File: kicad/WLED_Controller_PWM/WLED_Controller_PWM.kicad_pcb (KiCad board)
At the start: 2 copper layers, 72 x 50 mm, 45 parts, among them J1 USB_C_Receptacle_USB2.0, J2 Conn_01x03, J3 Conn_01x03, J4 Conn_01x03, J6 Conn_01x02, Q1 BC847, Q2 BC847, SW1 SW_RESET, SW2 SW_BOOT, SW3 SW_Push, U1 ESP32-WROOM-32, U2 CH340C, U3 NCP1117-3.3, U4 TSSP58P38, U5 74HC14

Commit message: Add PWM Controllers
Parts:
- removed C13: 100n, Capacitor_SMD:C_0603_1608Metric_Pad1.08x0.95mm_HandSolder
- removed J2, J3, J4: Conn_01x03, GioN_Custom:TerminalBlock_WAGO_236-403_1x03_P5.00mm_45Degree
- removed U5: 74HC14, Package_SO:SOIC-14_3.9x8.7mm_P1.27mm
- added J5: Conn_01x05, GioN_Custom:TerminalBlock_WAGO_236-405_1x05_P5.00mm_45Degree, F.Cu at (9.40, -31.9)
- added Q3: IRFL4105PBF, Package_TO_SOT_SMD:SOT-223, F.Cu at (22.9, -29.2)
- added Q4: IRFL4105PBF, Package_TO_SOT_SMD:SOT-223, F.Cu at (22.9, -21.3)
- added Q5: IRFL4105PBF, Package_TO_SOT_SMD:SOT-223, F.Cu at (22.9, -13.5)
- added Q6: IRFL4105PBF, Package_TO_SOT_SMD:SOT-223, F.Cu at (22.9, -5.59)
- added R13: 100R, Resistor_SMD:R_0603_1608Metric_Pad0.98x0.95mm_HandSolder, F.Cu at (29.0, -32.0)
- added R14: 10k, Resistor_SMD:R_0603_1608Metric_Pad0.98x0.95mm_HandSolder, F.Cu at (29.0, -26.4)
- added R15: 100R, Resistor_SMD:R_0603_1608Metric_Pad0.98x0.95mm_HandSolder, F.Cu at (29.0, -24.1)
- added R16: 10k, Resistor_SMD:R_0603_1608Metric_Pad0.98x0.95mm_HandSolder, F.Cu at (29.0, -18.5)
- added R17: 100R, Resistor_SMD:R_0603_1608Metric_Pad0.98x0.95mm_HandSolder, F.Cu at (29.0, -16.3)
- added R18: 10k, Resistor_SMD:R_0603_1608Metric_Pad0.98x0.95mm_HandSolder, F.Cu at (29.0, -10.7)
- added R19: 100R, Resistor_SMD:R_0603_1608Metric_Pad0.98x0.95mm_HandSolder, F.Cu at (29.0, -8.38)
- added R20: 10k, Resistor_SMD:R_0603_1608Metric_Pad0.98x0.95mm_HandSolder, F.Cu at (29.0, -2.79)
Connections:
- J6 pad 1: +5V -> +12V
- U1 pad 23: LED0 -> LED_R
- U1 pad 27: LED1 -> LED_G
- U1 pad 28: LED2 -> LED_B
- U1 pad 30: IO18 -> LED_W
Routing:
- net +5V: track 195.3 -> 48.2 mm
- net LED1: track 45.6 -> 0.00 mm, vias 2 -> 0
- net +12V: track 0.00 -> 44.9 mm
- net LED2: track 35.5 -> 0.00 mm, vias 2 -> 0
- net LED_G: track 0.00 -> 31.0 mm, vias 0 -> 2
- net LED_W: track 0.00 -> 29.6 mm, vias 0 -> 2
- net Net-(J4-Pin_2): track 27.2 -> 0.00 mm
- net LED_R: track 0.00 -> 26.7 mm, vias 0 -> 2
- net Net-(J3-Pin_2): track 25.8 -> 0.00 mm
- net LED_B: track 0.00 -> 25.0 mm, vias 0 -> 2
- net Net-(J2-Pin_2): track 22.2 -> 0.00 mm
- net Net-(J5-Pin_5): track 0.00 -> 20.9 mm
- net Net-(J5-Pin_4): track 0.00 -> 17.6 mm
- net LED0: track 17.1 -> 0.00 mm, vias 2 -> 0
- net Net-(J5-Pin_2): track 0.00 -> 16.3 mm
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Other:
- board text added: "+12V"
- board text added: "IO15 R"
- board text added: "IO16 G"
- board text added: "IO17 B"
- board text added: "IO18 W"
- board text added: "WLED Controller PWM V1 03/2024 Gioulekas Nikos"
- board text removed: "+5V"
- board text removed: "IO15 LED0"
- board text removed: "IO16 LED1"
- board text removed: "IO17 LED2"
- board text removed: "WLED Controller V1 02/2024 Gioulekas Nikos"

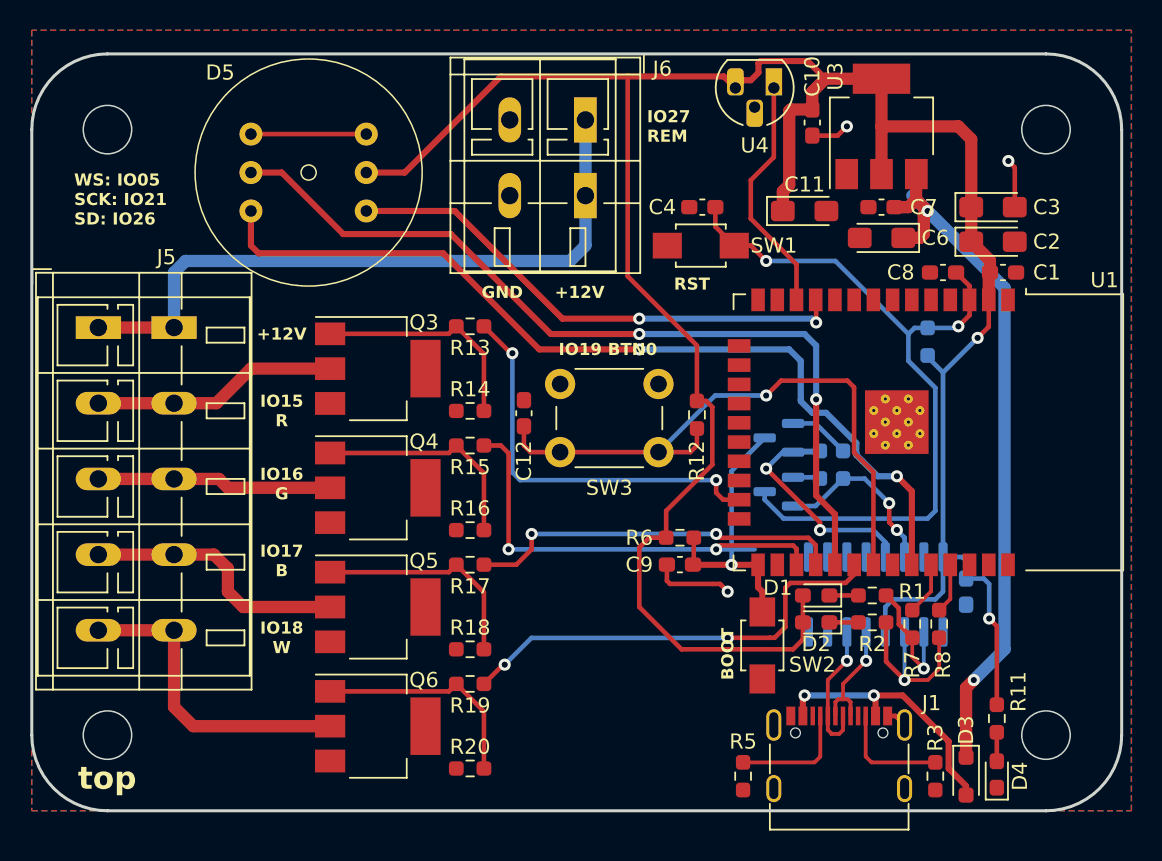
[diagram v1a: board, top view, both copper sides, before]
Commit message: add 7805
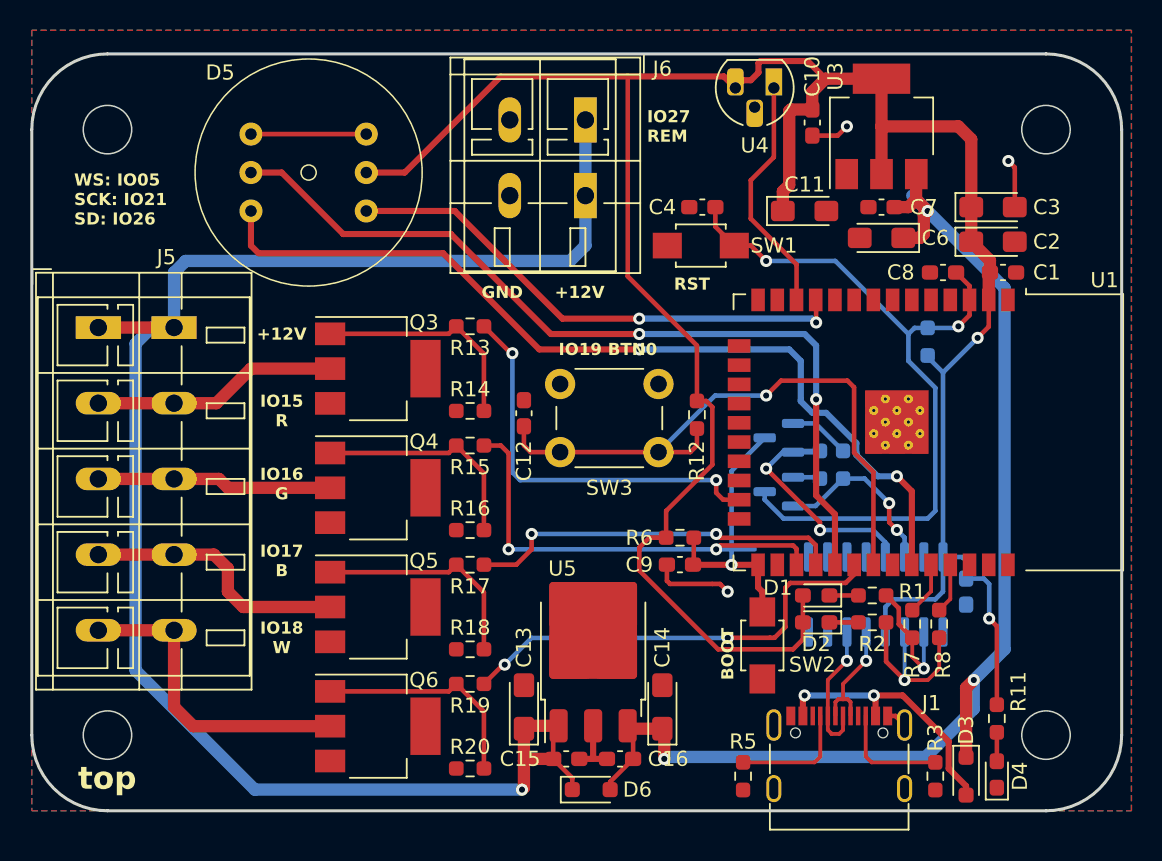
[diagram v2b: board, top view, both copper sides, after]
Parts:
- added C13: 10u, Capacitor_Tantalum_SMD:CP_EIA-3216-18_Kemet-A_Pad1.58x1.35mm_HandSolder, F.Cu at (32.5, -6.86)
- added C14: 10u, Capacitor_Tantalum_SMD:CP_EIA-3216-18_Kemet-A_Pad1.58x1.35mm_HandSolder, F.Cu at (41.7, -6.86)
- added C15: 100n, Capacitor_SMD:C_0603_1608Metric_Pad1.08x0.95mm_HandSolder, F.Cu at (35.3, -3.43)
- added C16: 100n, Capacitor_SMD:C_0603_1608Metric_Pad1.08x0.95mm_HandSolder, F.Cu at (38.9, -3.43)
- added D6: BAT60A, Diode_SMD:D_SOD-323_HandSoldering, F.Cu at (37.0, -1.40)
- added U5: L7805, Package_TO_SOT_SMD:TO-252-3_TabPin2, F.Cu at (37.1, -10.7)
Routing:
- net +12V: track 44.9 -> 111.5 mm, vias 0 -> 1
- net +5V: track 48.2 -> 81.3 mm, vias 2 -> 3
- net GND: track 20.1 -> 24.2 mm
- net +3.3V: track 169.2 -> 167.8 mm

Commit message: Change to WAGO250
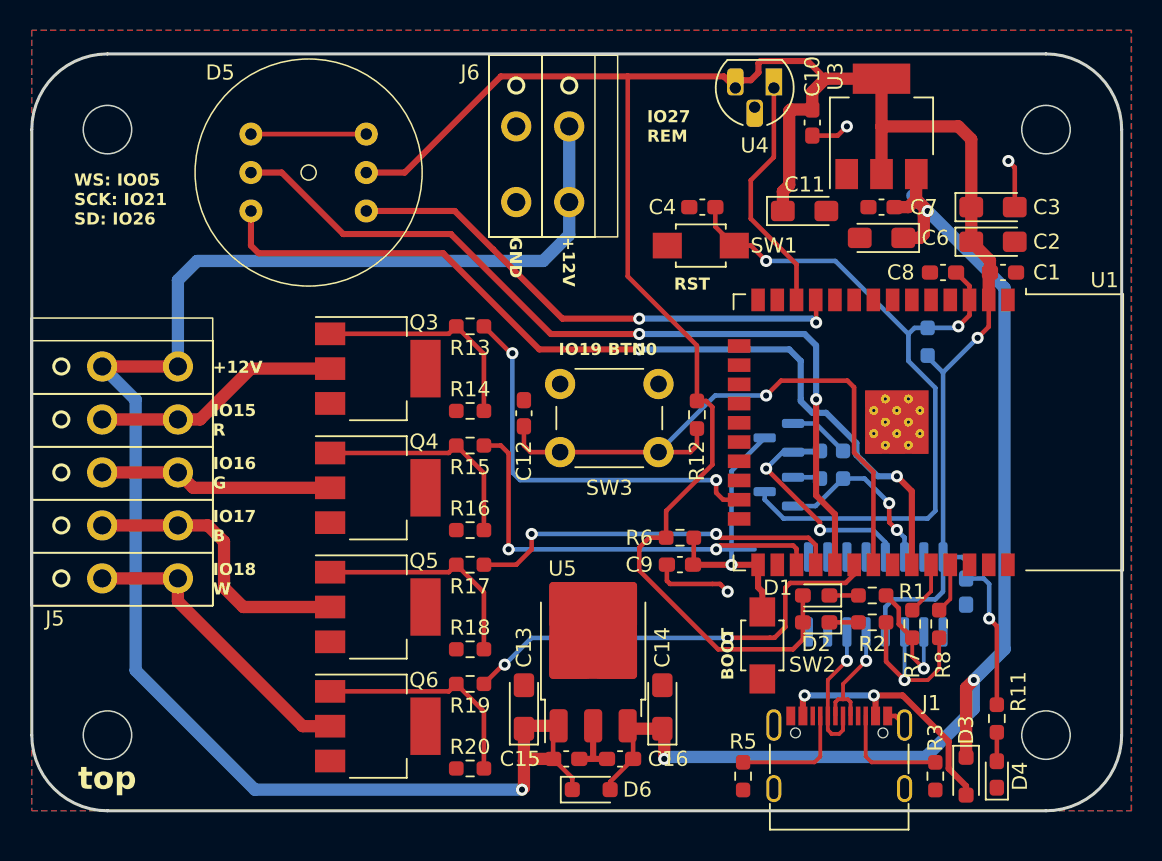
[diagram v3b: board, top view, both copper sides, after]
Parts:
- J5: footprint GioN_Custom:TerminalBlock_WAGO_236-405_1x05_P5.00mm_45Degree -> GioN_Custom:WAGO_250-205_1x05_P3.50mm
- J6: footprint GioN_Custom:TerminalBlock_WAGO_236-402_1x02_P5.00mm_45Degree -> GioN_Custom:WAGO_250-202_1x02_P3.50mm
- moved J5 18.5 mm to (12.0, -13.6)
- moved J6 6.93 mm to (30.2, -37.9)
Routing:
- net +12V: track 111.5 -> 108.1 mm
- net Net-(J5-Pin_4): track 17.6 -> 19.1 mm
- net Net-(J5-Pin_5): track 20.9 -> 20.0 mm

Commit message: Update WLED_Controller_PWM.kicad_pcb
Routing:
- net +5V: track 81.3 -> 79.9 mm
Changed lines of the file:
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@@
   (segment (start 59.055 -3.556) (end 41.91 -3.556) (width 0.8128) (layer "B.Cu") (net 4))
   (segment (start 64.262 -34.544) (end 59.182 -39.624) (width 0.8128) (layer "B.Cu") (net 4))
-  (segment (start 59.182 -39.624) (end 58.166 -40.64) (width 0.8128) (layer "B.Cu") (net 4))
   (segment (start 62.23 -6.731) (end 59.055 -3.556) (width 0.8128) (layer "B.Cu") (net 4))
   (segment (start 43.732 -18.04) (end 43.732 -16.312) (width 0.3048) (layer "F.Cu") (net 5))

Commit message: Add V1R1
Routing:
- net LED_G: track 31.0 -> 28.5 mm
- net +3.3V: track 167.8 -> 168.9 mm, vias 2 -> 3
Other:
- board text added: "WLED Controller PWM V1 R1 05/2024 Gioulekas Nikos"
- board text removed: "WLED Controller PWM V1 03/2024 Gioulekas Nikos"
